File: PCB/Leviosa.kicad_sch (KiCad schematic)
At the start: 59 parts, among them J1 Barrel_Jack, J2 2.54mm 1x03 Spare, Q1 NCE0110K, U1 TPS1H200AQDGNRQ1, U2 MC7805BD2TR4G, U3 SS495A, U4 MCP6001R, U5 LM393, U6 MX27517, U7 INA199xxDCK (50V/V), U8 STM32G030F6Px

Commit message: action items 2-5 on REV CHANGES.txt
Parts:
- added C15, C16: 0.1uF, Capacitor_SMD:C_1206_3216Metric, symbol Device:C
- added C17: 180pF, Capacitor_SMD:C_1206_3216Metric, symbol Device:C
- added R17: 3.9kΩ, Resistor_SMD:R_1206_3216Metric, symbol Device:R_US
- C10: value 47μF -> 0.1uF
- R15: value 0Ω -> 10Ω
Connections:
- net +12V: now also R11.1, R13.1; no longer C2.1, R1.2, U1.1 (IN), U1.2 (DIAG_EN), U1.8 (VS), U2.3 (VI)
- net COIL_OUT: now also L1.2; no longer R11.2, R14.1
- net CURT_SN: now also C16.2, R17.2; no longer U7.6
- net GND: now also C10.1, C15.1, C16.1, C17.1
- net GT_DRV: now also C17.2
- net at R14.2, U7.4 (+): now also C15.2; no longer C10.1
- new net: R1.2, R11.2, R14.1, U1.1 (IN), U1.2 (DIAG_EN), U1.8 (VS)
- new net: R17.1, U7.6
- new net: C2.1, U2.3 (VI)
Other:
- note added: "Coil Power Management"
- note added: "RC filter: R9 == R10 < 10Ω Fc = 1/ (2pi * R * C) let R = 10Ω and C = 180pF and C_gate = 690pF Fc = 18MHz"
- note added: "RC filter: R9 == R10 < 10Ω Fc = 1/ (2pi * R * C) let R = 3.9kΩ and C = 0.1μF Fc = 408Hz"
- note removed: "Power Management"
- moved on the sheet: 5V1, C1, C10, C11, C2, C4, D2, G1, L1, R1, R11, R13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

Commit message: added 10V and 3.3V LDO
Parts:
- removed D3: SS34, Diode_SMD:D_SOD-323, symbol Diode:SS34
- removed R10: 8.2Ω, Resistor_SMD:R_1206_3216Metric, symbol Device:R_US
- added C18: 20nF, Capacitor_SMD:C_0805_2012Metric_Pad1.18x1.45mm_HandSolder, symbol Device:C
- added C19: 0.1uF, Capacitor_SMD:C_1206_3216Metric, symbol Device:C
- added C20: 22µF, Capacitor_SMD:C_0805_2012Metric, symbol Device:C
- added C21: 10uF, Capacitor_SMD:C_0805_2012Metric, symbol Device:C
- added D1: SS34, Diode_SMD:D_SOD-323, symbol Diode:SS34
- added J3: Conn_01x05_Socket, Connector_PinHeader_2.54mm:PinHeader_1x05_P2.54mm_Vertical, symbol Connector:Conn_01x05_Socket
- added R18: 8.2Ω, Resistor_SMD:R_1206_3216Metric, symbol Device:R_US
- added U10: AZ1117CH2-3.3, Package_TO_SOT_SMD:SOT-223-3_TabPin2, symbol Regulator_Linear:AZ1117CH2-3.3
- added U9: L78L10_SOT89, Package_TO_SOT_SMD:SOT-89-3, symbol Regulator_Linear:L78L10_SOT89
- C9: value 20nF -> 0.33µF; footprint Capacitor_SMD:C_0805_2012Metric_Pad1.18x1.45mm_HandSolder -> Capacitor_SMD:C_0805_2012Metric; Link https://jlcpcb.com/partdetail/1954-0603B203K500NT/C1602 -> https://jlcpcb.com/partdetail/74255-CL21B334KBFNNNE/C73142
- G1: value set_point_trigger -> GT_DRV
- renumbered L1 to COIL1
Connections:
- net +12V_SF: now also C18.2, D1.1 (K), U9.3 (IN)
- net +5V: no longer C12.1, C14.1, C3.1, C5.1, C6.1, C7.1, R4.2, R6.2, R9.2, SRV1.2 (Pin_2), SRV2.2 (Pin_2), U3.1 (VCC), U4.2 (V+), U5.8 (V+)
- net COIL_OUT: now also C18.1, R18.2; no longer C9.2
- net GND: now also C14.1, C3.1, C9.2, U8.5 (VSS), C19.1, C20.2, C21.2, J3.5 (Pin_5), U10.2 (GND), U9.2 (GND)
- net INST_OUT_F: now reaches C8.2, R8.2, U5.3 (+), U5.6 (-)
- net +3.3V: now reaches C14.2
- net +3.3V: now also C3.2, C5.1, C6.1, SRV1.2 (Pin_2), SRV2.2 (Pin_2), U8.4 (VDD), C20.1, U10.3 (OUT)
- net SWDIO: now reaches U8.18 (PA13)
- net SWDIO: now also J3.3 (Pin_3)
- net SWCLK: now reaches U8.19 (PA14/PA15)
- net SWCLK: now also J3.2 (Pin_2)
- net NRST: now reaches U8.6 (NRST)
- net NRST: now also J3.4 (Pin_4)
- net DRV_OUT: now reaches R15.1, U6.6 (OUT)
- net HALL renamed HALL_OUT
- new net: D1.2 (A), R18.1
- new net +10V: C12.1, C19.2, C21.1, C7.1, R4.2, R6.2, R9.2, U10.1 (IN), U3.1 (VCC), U4.2 (V+), U5.8 (V+), U9.1 (OUT)
- new net +3V3: J3.1 (Pin_1)
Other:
- note added: "100mA should be enough from what I could see"
- note added: "Check this is right orientation"
- note added: "Need re calc"
- note added: "Need re calc?"
- note added: "Should we increase this to the 100v/v or 200v/v version?"
- note added: "This one by TI it should be good Have no fear"
- note removed: "RC filter: R9 == R10 < 10Ω Fc = 1/ (2pi * R * C) let R = 8Ω and Fc = 500Hz C = 1/ (2pi * R * Fc) = 40μF"
- note removed: "R_shunt: LR2010-21R050F2 - chat tells me: - ~50mΩ - min 0.05W power dissapation"
- moved on the sheet: C12, C13, C14, C17, C3, C5, C6, C7, C8, COIL1, D4, FID1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

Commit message: Added firmware, cleaned up schematic
Changed curr_sns resistor to 0603 since output is voltage not current related

Changed 3.9K to 3K9 for all resistors

Added LEDS found at home for 12, 10 and 3.3

Changed components to run off 10V and 3.3 when possible

Voltage dividers for setpoint need re calculating

Added Test points

Added supplier field to some ICs
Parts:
- removed 12V1: 12V, TestPoint:TestPoint_Pad_D1.0mm, symbol Connector:TestPoint
- removed 5V1: 5V, TestPoint:TestPoint_Pad_D1.5mm, symbol Connector:TestPoint
- removed C2, C4: 0.33µF, Capacitor_SMD:C_0805_2012Metric, symbol Device:C
- removed U2: MC7805BD2TR4G, Package_TO_SOT_SMD:TO-263-2, symbol Regulator_Linear:AMS1117-5.0
- added D2, D3: LED, LED_SMD:LED_0603_1608Metric, symbol Device:LED
- added R10: 240R, Resistor_SMD:R_0603_1608Metric, symbol Device:R_US
- added R9: 1K47, Resistor_SMD:R_0603_1608Metric, symbol Device:R_US
- added TP1: 12V, TestPoint:TestPoint_Pad_D1.0mm, symbol Connector:TestPoint
- added TP3: 10V, TestPoint:TestPoint_Pad_D1.0mm, symbol Connector:TestPoint
- added TP4: 3V3, TestPoint:TestPoint_Pad_D1.0mm, symbol Connector:TestPoint
- D4: footprint LED_SMD:LED_0805_2012Metric -> LED_SMD:LED_0603_1608Metric; Colour (none) -> Green; MANUFACTURER Luminus Devices Inc. -> (none); MAXIMUM_PACKAGE_HEIGHT 0.52 mm -> (none); PARTREV 16 -> (none); STANDARD Manufacturer Recommendations -> (none); Supplier (none) -> https://www.lcsc.com/product-detail/C19712532.html?s_z=n_sz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; Vf 2.2V -> 3.1V
- R12: renamed from R5; value 3.9kΩ -> 3K9
- R16: renamed from R9; value 3.9kΩ -> 3K9
- R5: renamed from R2; value 3.9kΩ -> 3K9
- R6: renamed from R17; value 3.9kΩ -> 3K9; footprint Resistor_SMD:R_1206_3216Metric -> Resistor_SMD:R_0603_1608Metric
- R7: renamed from R3; value 2kΩ -> 3K9
- R8: renamed from R16; value 2kΩ -> 3K9
- TP2: renamed from VO1; value Vout -> 12_Safe
- TP6: renamed from TP_COIL1; value Coil Output -> COIL_OUT
- U1: renamed from U8; Supplier (none) -> https://www.lcsc.com/product-detail/C529330.html
- U3: renamed from U7; value INA199xxDCK (50V/V) -> INA199A1DCKR; Supplier (none) -> https://www.lcsc.com/product-detail/C59135.html?s_z=n_INA199
- renumbered C14 to C1, C6 to C10, C19 to C11, C21 to C12, C7 to C13, C20 to C14, C12 to C15, C8 to C16, C13 to C17, C17 to C18, C18 to C19, C3 to C2, C10 to C3, C15 to C4, C11 to C5, C1 to C6, C16 to C7, C9 to C8, C5 to C9, D2 to D1, D1 to D5, J3 to J2, J2 to J3, R11 to R1, R4 to R11, R8 to R13, R6 to R14, R7 to R15, R12 to R17, R15 to R18, R18 to R19, R1 to R2, R13 to R3, R14 to R4, G1 to TP5, U1 to U2, U9 to U4, U10 to U5, U3 to U6, U4 to U7, U5 to U8, U6 to U9
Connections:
- net +10V: now also C17.1, U9.1 (VCC), R9.1, TP3.1; no longer C15.1, U7.2 (V+)
- net +12V: now also TP1.1
- net +3.3V: now also C15.1, C5.1, U3.3 (V+), U7.2 (V+), R10.1, TP4.1
- net COIL_OUT: now also D2.1 (K); no longer D4.1 (K)
- net CURT_SN: now also U1.11 (PA4)
- net FAULT: now also U1.14 (PA7); no longer U1.7 (PA0)
- net GND: now also D4.1 (K), D3.1 (K)
- net SVR1_CTRL: now also U1.13 (PA6)
- net SVR2_CTRL: now also U1.20 (PB3/PB4/PB5/PB6)
- net at R8.2: now also D2.2 (A); no longer D4.2 (A)
- removed net +5V: C17.1, C5.1, U3.3 (V+), U9.1 (VCC)
- new net: D3.2 (A), R9.2
- new net: D4.2 (A), R10.2
- no-connect marks 1 -> 2
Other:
- note added: "(10-3.3)*0.1A = 0.67W 0.67W *125C/W + 25C = 109C 150C max"
- note added: "(12-10)*0.1A = 0.2W 0.2W * 55C/W = 36C"
- note added: "(12V - 9.6V)/5ma = 460 Ohm"
- note added: "MCU"
- note removed: "(12V - 9.6V)/5ma = 460 Ohm min"
- note removed: "100mA should be enough from what I could see"
- note removed: "Check this is right orientation"
- note removed: "Digital Circuit"
- note removed: "Input Ref"
- note removed: "Need re calc?"
- note removed: "Should we increase this to the 100v/v or 200v/v version?"
- note removed: "This one by TI it should be good Have no fear"
- moved on the sheet: C1, C10, C11, C12, C13, C14, C15, C16, C17, C18, C19, C2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

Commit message: swap instrumental amp
swap MCP6001 to LM321 to allow for higher output voltage:
   (V+)-(V-) = 7V --> 36V
(similar for inputs)
note component has slightly slower slew rate
checked pinout
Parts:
- removed U7: MCP6001R, Package_TO_SOT_SMD:SOT-23-5, symbol Amplifier_Operational:MCP6001R
- added U10: LM321, Package_TO_SOT_SMD:SOT-23-5, symbol Amplifier_Operational:LM321
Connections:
- net +3.3V: now also U10.5 (V+)
- net GND: now also U10.2 (V-)
- net HALL_OUT: now also U10.1 (+)
- net INST_OUT: now also U10.3 (-), U10.4
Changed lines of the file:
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@@
-	)
-	(symbol
-		(lib_id "Amplifier_Operational:MCP6001R")
-		(at 222.25 232.41 0)
-		(unit 1)
-		(exclude_from_sim no)
-		(in_bom yes)
-		(on_board yes)
-		(dnp no)
-		(property "Reference" "U7"
-			(at 223.52 226.06 0)
-			(effects
-				(font
-					(size 1.27 1.27)
-				)
-			)
-		)
-		(property "Value" "MCP6001R"
-			(at 227.33 228.6 0)
-			(effects
-				(font
-					(size 1.27 1.27)
-				)
-			)
-		)
-		(property "Footprint" "Package_TO_SOT_SMD:SOT-23-5"
-			(at 222.25 232.41 0)
-			(effects
-				(font
-					(size 1.27 1.27)
-				)
-				(hide yes)
-			)
-		)
-		(property "Datasheet" "https://ww1.microchip.com/downloads/en/DeviceDoc/MCP6001-1R-1U-2-4-1-MHz-Low-Power-Op-Amp-DS20001733L.pdf"
-			(at 222.25 227.33 0)
-			(effects
-				(font
-					(size 1.27 1.27)
-				)
-				(hide yes)
-			)
-		)
-		(property "Description" "1MHz, Low-Power Op Amp, SOT-23-5"
-			(at 222.25 232.41 0)
-			(effects
-				(font
-					(size 1.27 1.27)
-				)
-				(hide yes)
-			)
-		)
-		(property "Link" "https://jlcpcb.com/partdetail/5767612-MCP6001AIDBVRG/C5145245"
-			(at 222.25 232.41 0)
-			(effects
-				(font
-					(size 1.27 1.27)
-				)
-				(hide yes)
-			)
-		)
-		(pin "5"
-		)
-		(pin "2"
-		)
-		(pin "1"
-		)
-		(pin "4"
-		)
-		(pin "3"
-		)
-		(instances
-			(project ""
-				(path "/fe766911-203b-467c-b704-d4bd488f6c98"
-					(reference "U7")
-					(unit 1)
-				)
-			)
-		)
 	)
 	(symbol
@@
 					(unit 1)
 				)
+			)
+		)
+	)
+	(symbol
+		(lib_id "Amplifier_Operational:LM321")
+		(at 222.25 232.41 0)
+		(unit 1)
+		(exclude_from_sim no)
+		(in_bom yes)
+		(on_board yes)
+		(dnp no)
+		(property "Reference" "U10"
+			(at 225.044 225.044 0)
+			(effects
+				(font
+					(size 1.27 1.27)
+				)
+			)
+		)
+		(property "Value" "LM321"
+			(at 225.044 227.584 0)
+			(effects
+				(font
+					(size 1.27 1.27)
+				)
+			)
+		)
+		(property "Footprint" "Package_TO_SOT_SMD:SOT-23-5"
+			(at 222.25 232.41 0)
+			(effects
+				(font
+					(size 1.27 1.27)
+				)
+				(hide yes)
+			)
+		)
+		(property "Datasheet" "http://www.ti.com/lit/ds/symlink/lm321.pdf"
+			(at 222.25 232.41 0)
+			(effects
+				(font
+					(size 1.27 1.27)
+				)
+				(hide yes)
+			)
+		)
+		(property "Description" "Low Power Single Operational Amplifier, SOT-23-5"
+			(at 222.25 232.41 0)
+			(effects
+				(font
+					(size 1.27 1.27)
+				)
+				(hide yes)
+			)
+		)
+		(property "Source1" "https://www.lcsc.com/product-detail/C9405.html?spm=wm.fly.bg.14.stp&lcsc_vid=FFkIV1BTRQcNBl1TFFkLUFMETlUKUVIARFYLA1wDFAUxVlNRQ1VdXlZXQFZZUzsOAxUeFF5JWBYZEEoKFBINSQcJGk4dAgUUFAk%3D"
+			(at 222.25 232.41 0)
+			(effects
+				(font
+					(size 1.27 1.27)
+				)
+				(hide yes)
+			)
+		)
+		(pin "3"
+		)
+		(pin "5"
+		)
+		(pin "2"
+		)
+		(pin "1"
+		)
+		(pin "4"
+		)
+		(instances
+			(project ""
+				(path "/fe766911-203b-467c-b704-d4bd488f6c98"
+					(reference "U10")
+					(unit 1)
+				)

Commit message: update footprint for schottkey diode (SS34)
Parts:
- D5: footprint Diode_SMD:D_SOD-323 -> Diode_SMD:D_SMA_Handsoldering
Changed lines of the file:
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@@
 			)
 		)
-		(property "Footprint" "Diode_SMD:D_SOD-323"
+		(property "Footprint" "Diode_SMD:D_SMA_Handsoldering"
 			(at 343.535 172.72 0)
 			(effects

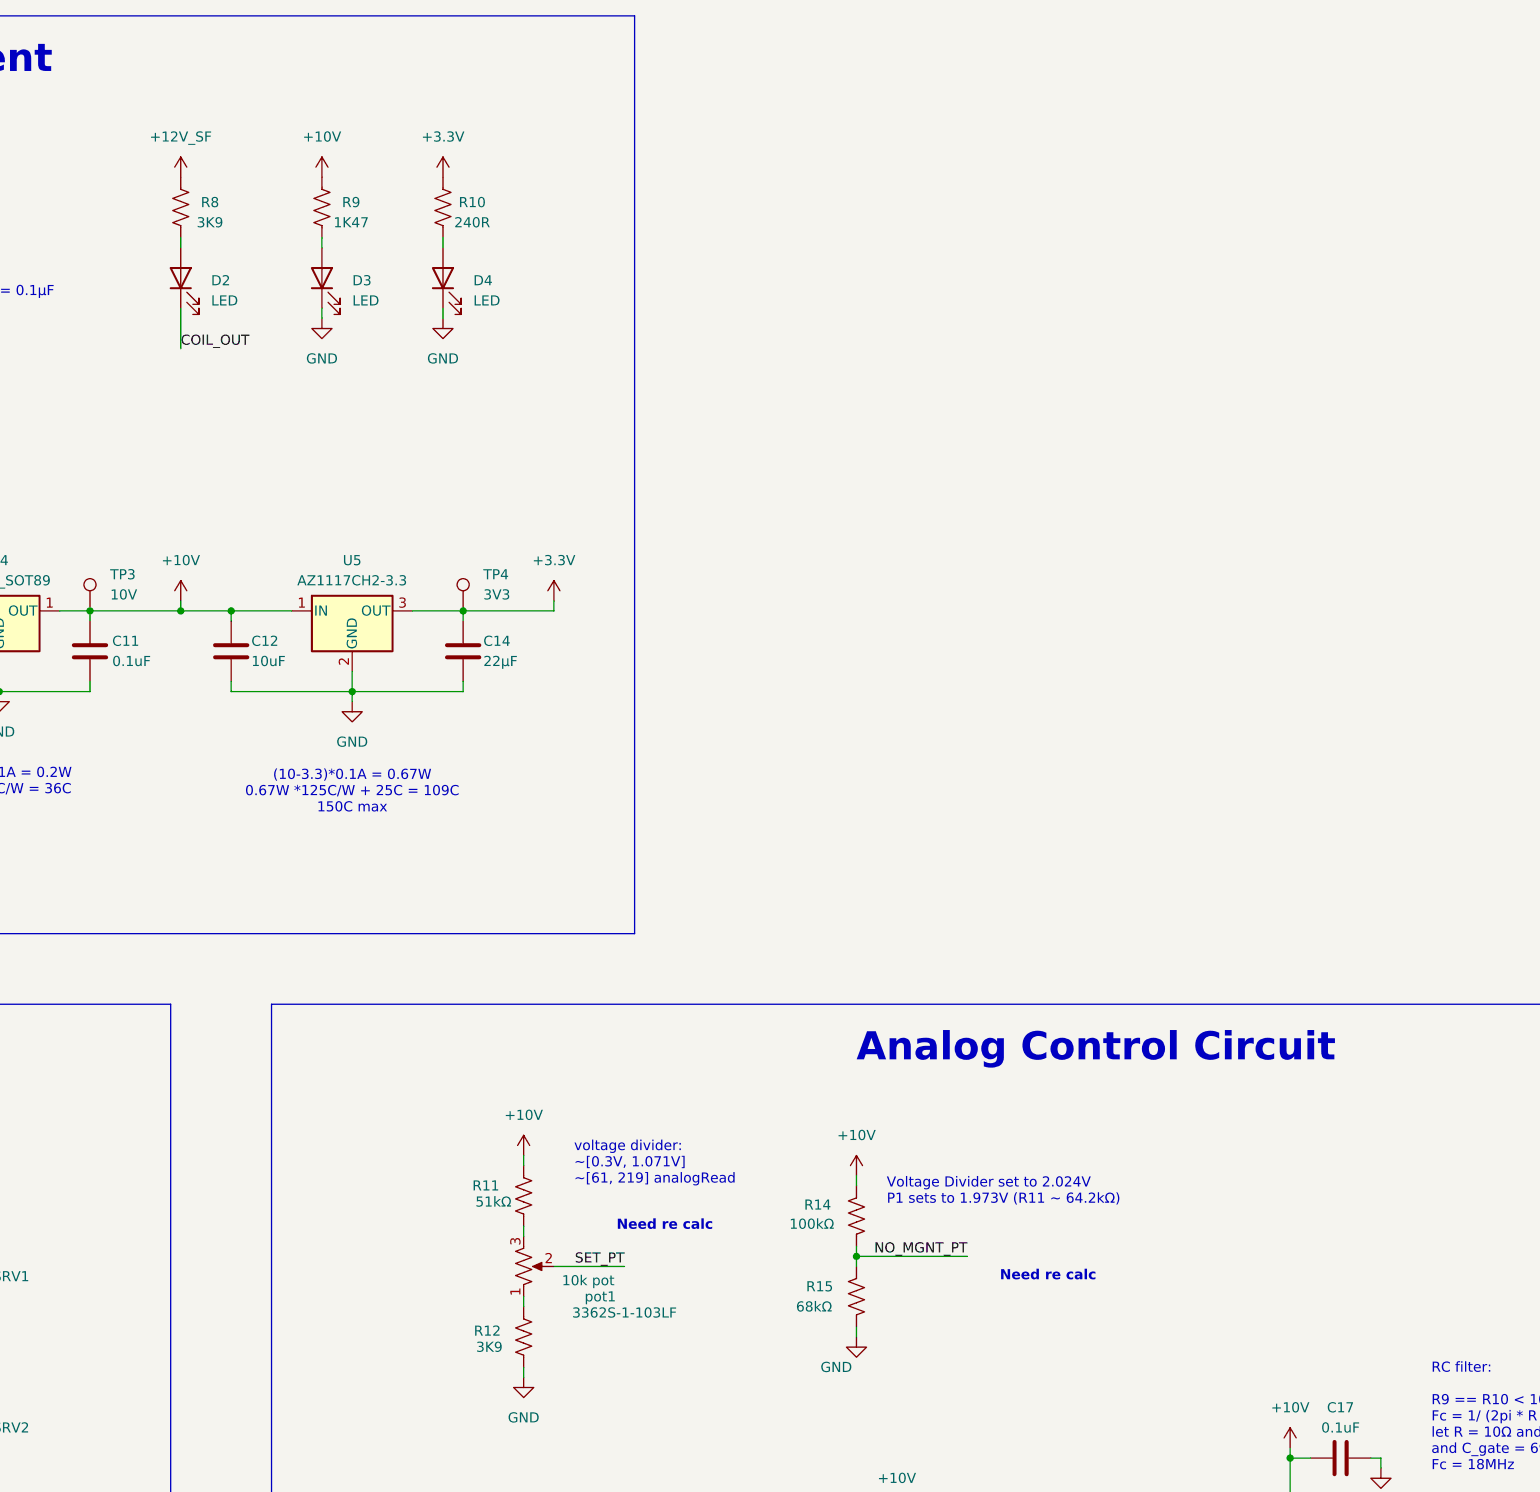
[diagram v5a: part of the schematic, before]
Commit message: add zener diode to 10V LED indicator, shift coil indicator to analog control circuit section
For current limiting resistors on 10V LED indicator:
Min resistance: (10-6.2-3.1)/0.005 = 140R --> choose 480R (doubled up on 240R)

For current limiting resistor on 3V3 LED indicator:
Min resistance: (3.3-3.1)/0.005 = 40R --> choose 240R (didn't change)
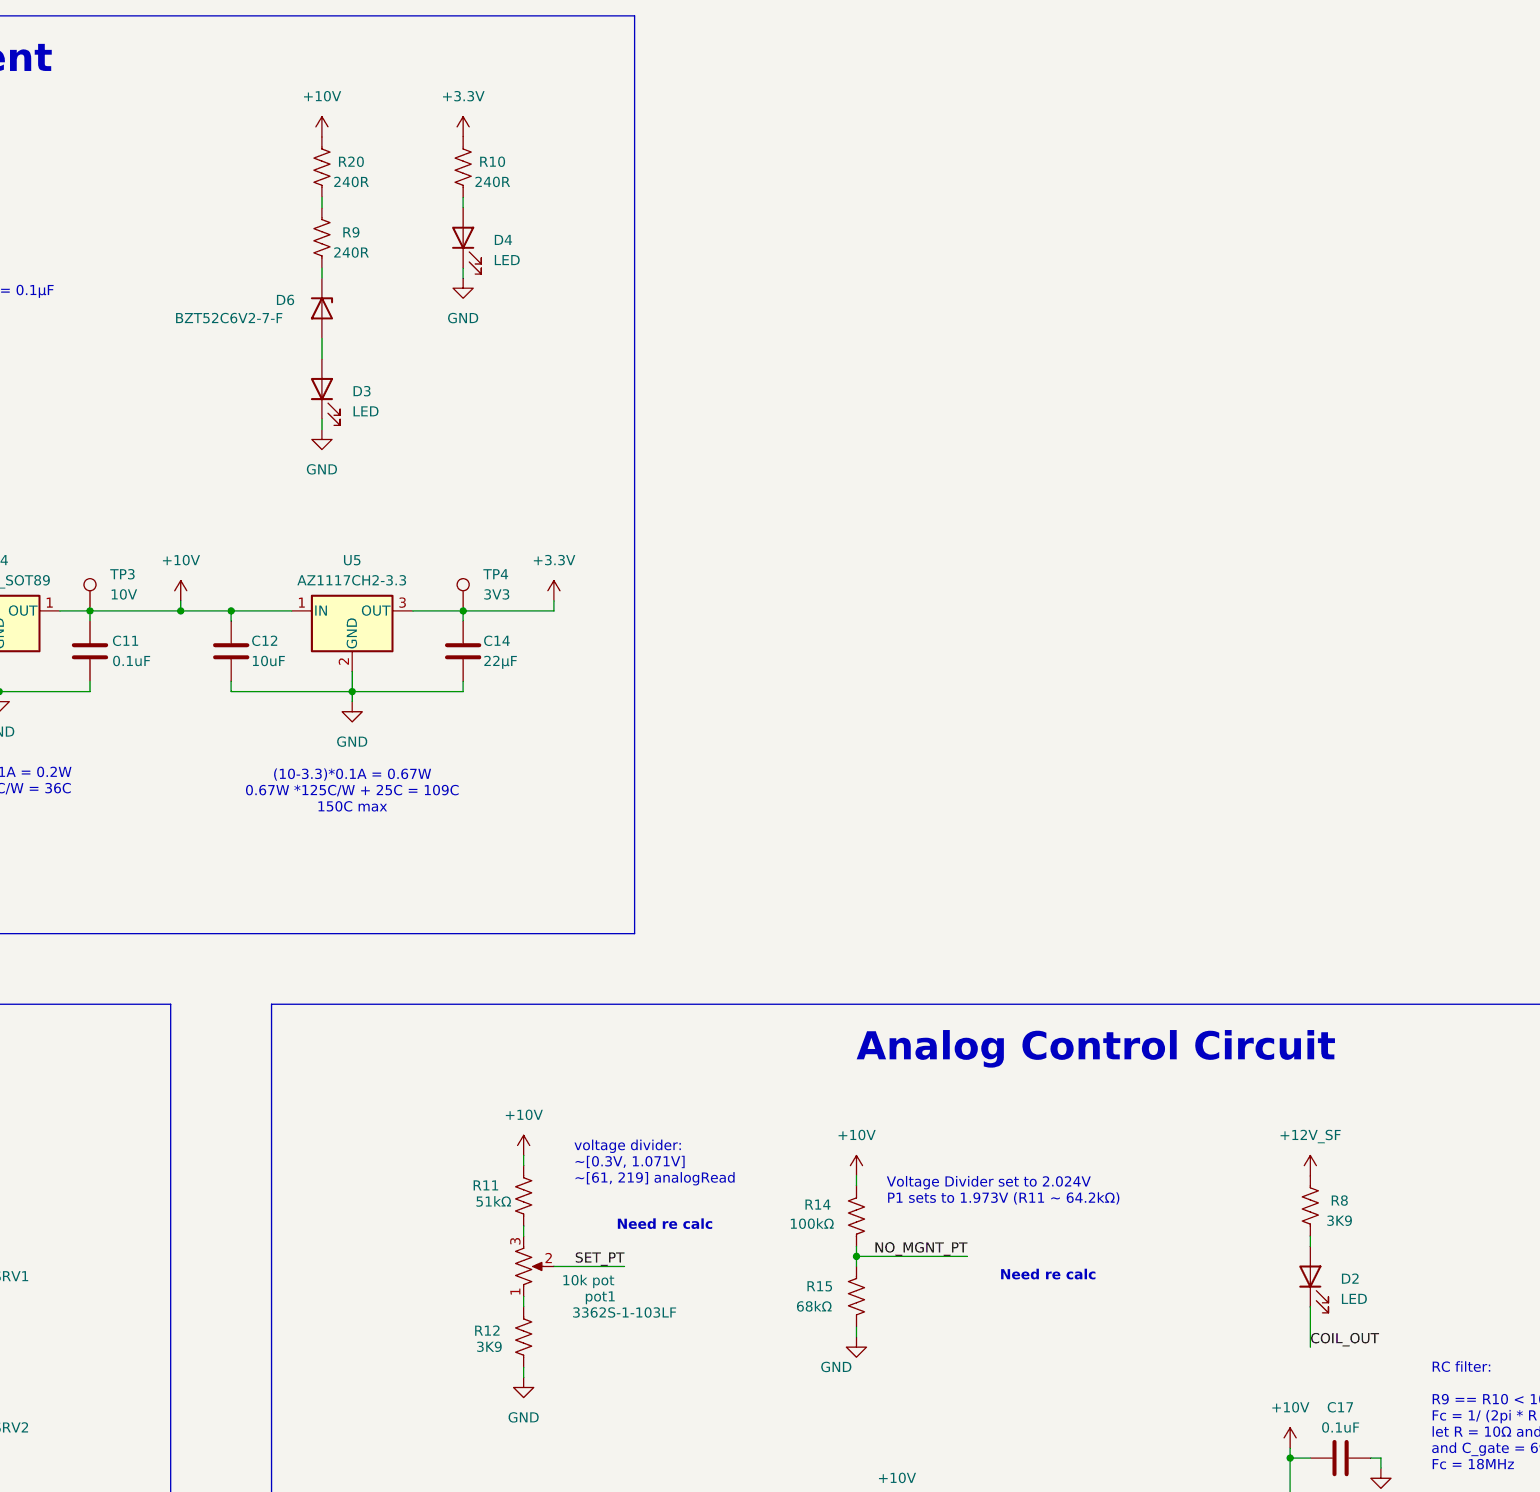
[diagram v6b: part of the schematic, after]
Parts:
- added D6: BZT52C6V2-7-F, Diode_SMD:D_SOD-123, symbol Device:D_Zener
- added R20: 240R, Resistor_SMD:R_0603_1608Metric, symbol Device:R_US
- D5: Link2 (none) -> https://www.lcsc.com/product-detail/C8678.html?s_z=n_SS34&s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
- R9: value 1K47 -> 240R
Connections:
- net +10V: now also R20.1; no longer R9.1
- net at R9.2: now also D6.1 (K); no longer D3.2 (A)
- new net: D3.2 (A), D6.2 (A)
- new net: R20.2, R9.1
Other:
- moved on the sheet: D2, D3, D4, R10, R8
